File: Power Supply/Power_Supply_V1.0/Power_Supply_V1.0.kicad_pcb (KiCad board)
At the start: 2 copper layers, 165.1 x 67.3 mm, 43 parts

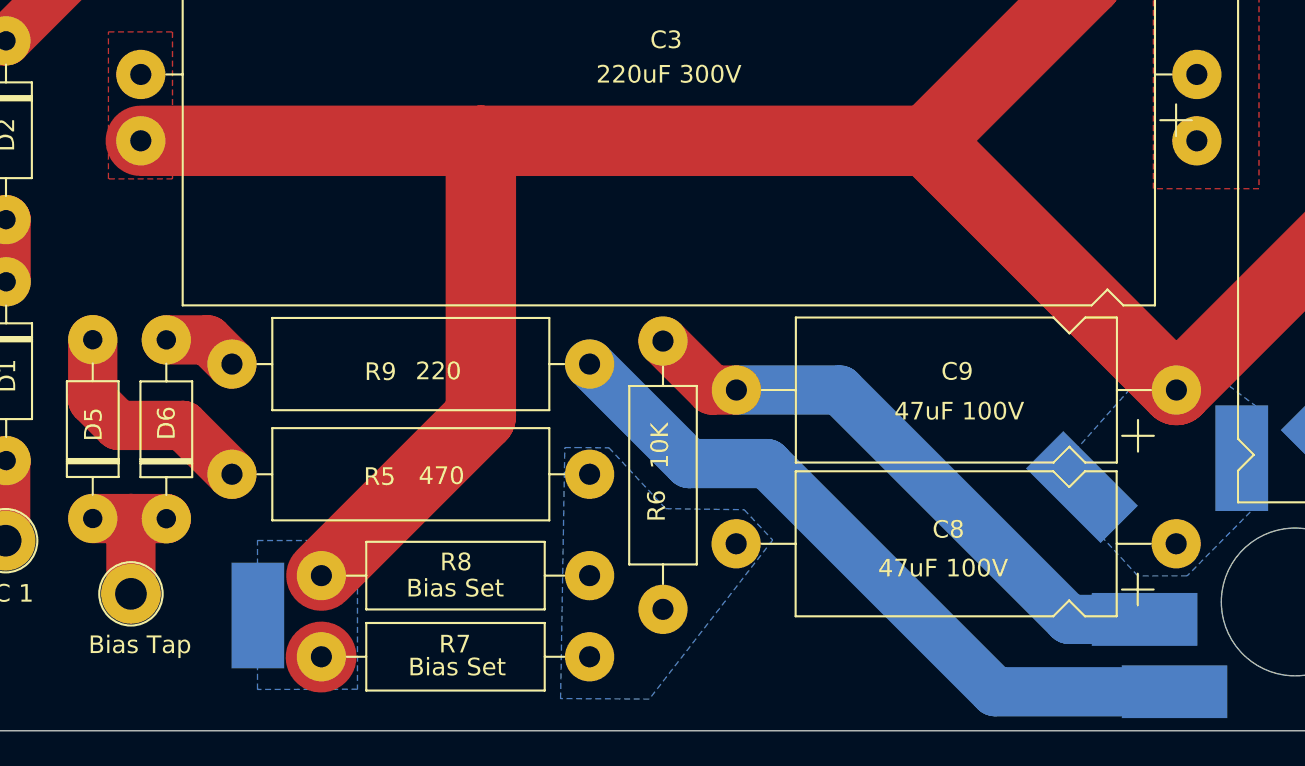
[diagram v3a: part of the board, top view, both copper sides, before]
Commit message: Adjusted Resistor Sizes
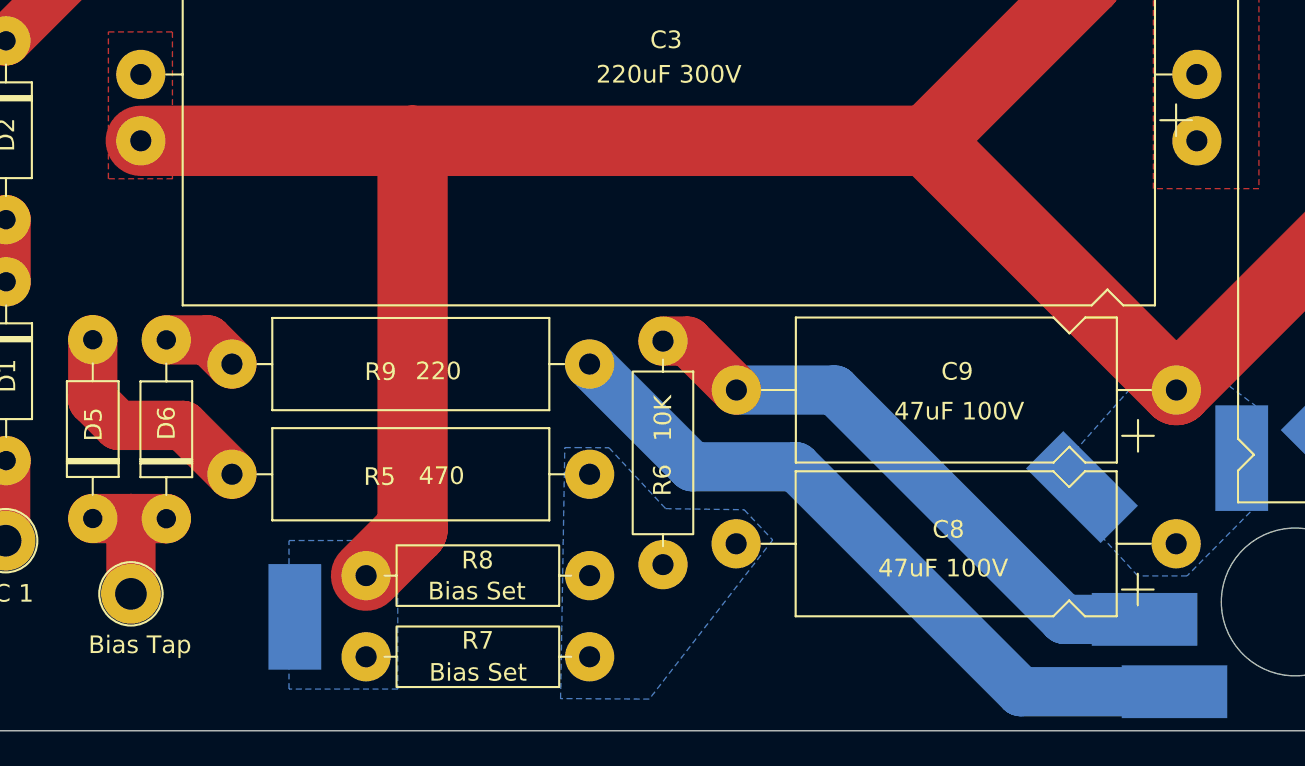
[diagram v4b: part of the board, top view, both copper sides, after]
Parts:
- R6, R7, R8: footprint Resistor_THT:R_Axial_DIN0411_L9.9mm_D3.6mm_P15.24mm_Horizontal -> Resistor_THT:R_Axial_DIN0309_L9.0mm_D3.2mm_P12.70mm_Horizontal
- moved TP6 2.10 mm to (81.8, 130.6)
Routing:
- net GND: track 164.6 -> 161.9 mm
